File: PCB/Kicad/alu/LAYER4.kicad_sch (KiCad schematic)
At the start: 4 parts, among them U41 74LS257, U42 74LS257, U43 74LS257, U44 74LS257

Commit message: UPDATE
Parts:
- added C38, C39, C40, C41: 10n, symbol Device:C
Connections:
- net GND: now also U43.10 (I1d), U43.13 (I1c), U43.3 (I1a), U43.6 (I1b), U44.13 (I1c), U44.3 (I1a), U44.6 (I1b), C38.2, C39.2, C40.2, C41.2
- net Lin1: no longer U41.3 (I1a)
- net Lin10: now also U41.13 (I1c); no longer U43.6 (I1b)
- net Lin11: now also U41.10 (I1d); no longer U43.13 (I1c)
- net Lin12: now also U42.3 (I1a); no longer U43.10 (I1d)
- net Lin13: now also U42.6 (I1b); no longer U44.3 (I1a)
- net Lin14: now also U42.13 (I1c); no longer U44.6 (I1b)
- net Lin15: now also U42.10 (I1d); no longer U44.13 (I1c)
- net Lin2: no longer U41.6 (I1b)
- net Lin3: no longer U41.13 (I1c)
- net Lin4: no longer U41.10 (I1d)
- net Lin5: no longer U42.3 (I1a)
- net Lin6: no longer U42.6 (I1b)
- net Lin7: no longer U42.13 (I1c)
- net Lin8: now also U41.3 (I1a); no longer U42.10 (I1d)
- net Lin9: now also U41.6 (I1b); no longer U43.3 (I1a)
- net VCC: now also C38.1, C39.1, C40.1, C41.1

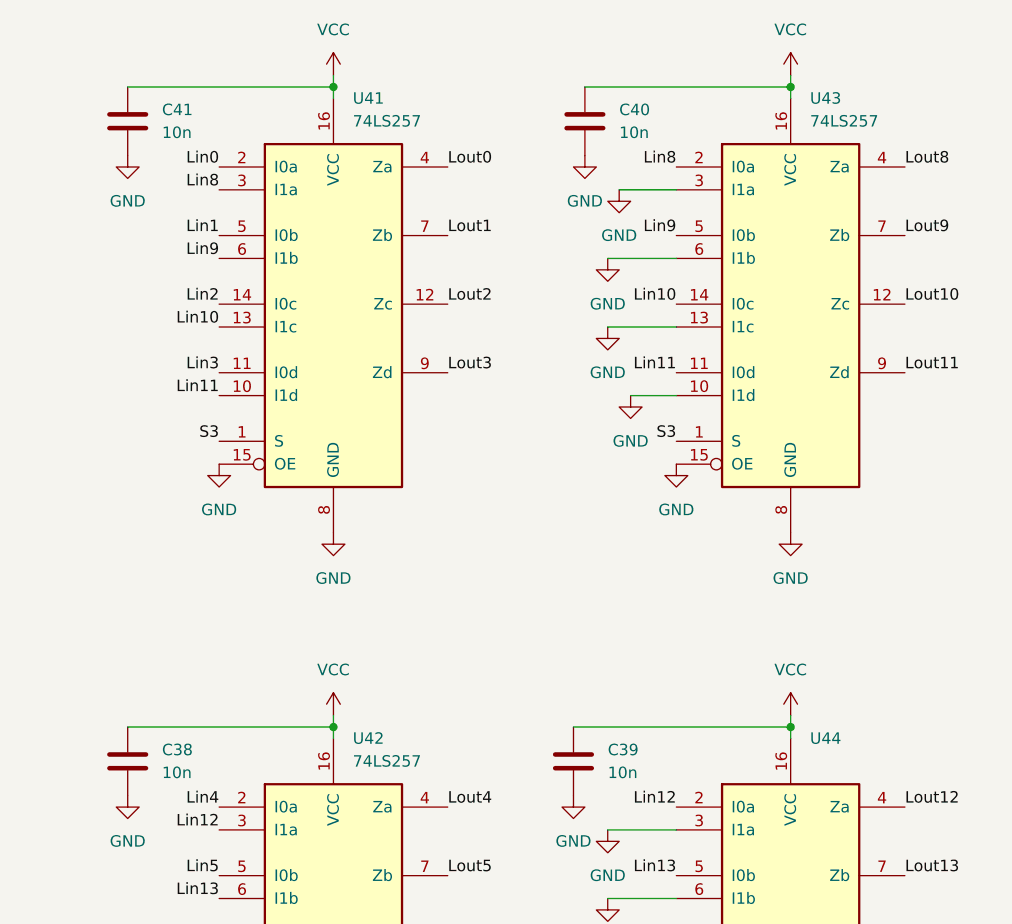
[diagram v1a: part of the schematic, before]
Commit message: LEDs added
REGISTER.kicad_sch LEDs added to both REG_A and REG_B
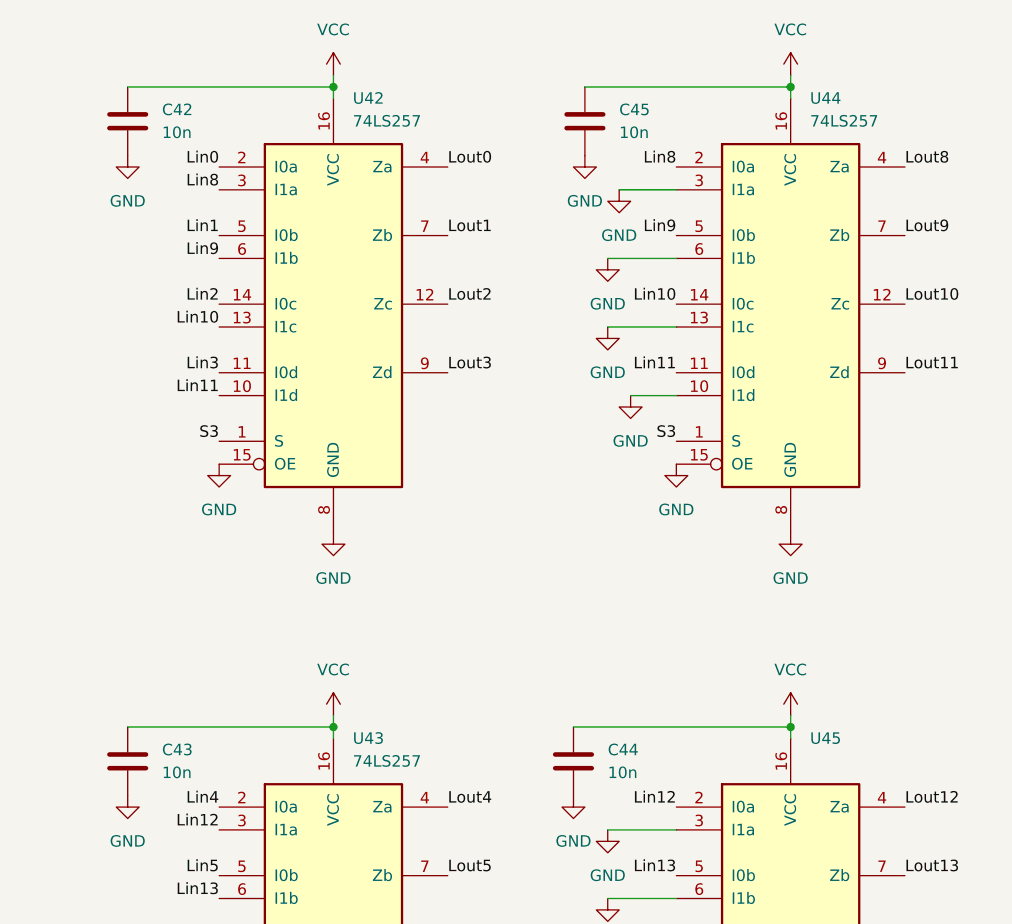
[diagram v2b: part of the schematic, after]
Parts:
- renumbered C41 to C42, C38 to C43, C39 to C44, C40 to C45, U41 to U42, U42 to U43, U43 to U44, U44 to U45

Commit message: Footprints, PCB update
Added footprints to all components, updated the PCB with the schematic
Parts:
- C42, C43, C44, C45: footprint (none) -> Capacitor_SMD:C_0603_1608Metric
- U42, U43, U44, U45: footprint (none) -> Package_SO:SOIC-16_3.9x9.9mm_P1.27mm
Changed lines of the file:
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@@
 			)
 		)
-		(property "Footprint" ""
+		(property "Footprint" "Capacitor_SMD:C_0603_1608Metric"
 			(at 98.7552 46.99 0)
 			(effects
@@
 			)
 		)
-		(property "Footprint" ""
+		(property "Footprint" "Capacitor_SMD:C_0603_1608Metric"
 			(at 149.5552 46.99 0)
 			(effects
@@
 			)
 		)
-		(property "Footprint" ""
+		(property "Footprint" "Package_SO:SOIC-16_3.9x9.9mm_P1.27mm"
 			(at 171.45 63.5 0)
 			(effects
@@
 			)
 		)
-		(property "Footprint" ""
+		(property "Footprint" "Package_SO:SOIC-16_3.9x9.9mm_P1.27mm"
 			(at 120.65 134.62 0)
 			(effects
@@
 			)
 		)
-		(property "Footprint" ""
+		(property "Footprint" "Capacitor_SMD:C_0603_1608Metric"
 			(at 148.2852 118.11 0)
 			(effects
@@
 			)
 		)
-		(property "Footprint" ""
+		(property "Footprint" "Package_SO:SOIC-16_3.9x9.9mm_P1.27mm"
 			(at 120.65 63.5 0)
 			(effects
@@
 			)
 		)
-		(property "Footprint" ""
+		(property "Footprint" "Package_SO:SOIC-16_3.9x9.9mm_P1.27mm"
 			(at 171.45 134.62 0)
 			(effects
@@
 			)
 		)
-		(property "Footprint" ""
+		(property "Footprint" "Capacitor_SMD:C_0603_1608Metric"
 			(at 98.7552 118.11 0)
 			(effects

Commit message: ALU Pcb update
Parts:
- C42, C43, C44, C45: value 10n -> 100nF; footprint Capacitor_SMD:C_0603_1608Metric -> Capacitor_SMD:C_0402_1005Metric
- U42, U43, U44, U45: value 74LS257 -> 74257
